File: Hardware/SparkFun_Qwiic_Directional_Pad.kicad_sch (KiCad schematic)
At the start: 36 parts, among them J1 Qwiic_RA, J2 Conn_01x04, J3 Qwiic_RA, J5 I2C, SW2 Nav Switch, U4 PCA9557PW

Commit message: Add ignore
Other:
- note added: "Default I²C Address: 0x18"
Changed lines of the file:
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@@
+		)
+	)
+	(text "Default I²C Address: 0x18"
+		(exclude_from_sim no)
+		(at 190.5 86.36 0)
+		(effects
+			(font
+				(size 1.27 1.27)
+			)
 		)
 	)

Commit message: Fix page names.
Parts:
- added JP6: I²C, SparkFun-Jumper:Jumper_3_NC-2_Trace, symbol SparkFun-Jumper:SolderJumper_3_Bridged123
- added R13, R7: 2.2k, SparkFun-Resistor:R_0603_1608Metric, symbol SparkFun-Resistor:2.2k_0603
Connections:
- net 3.3V: now also JP6.2 (C)
- net SCL: now also R7.2
- net SDA: now also R13.2
- new net: JP6.1 (A), R13.1
- new net: JP6.3 (B), R7.1
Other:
- title: RTK Postcard Portable Shield -> SparkFun Qwiic Directional Pad
- moved on the sheet: C1, D1, D4, J1, J2, J3, J5, JP1, JP2, JP3, R1, R10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

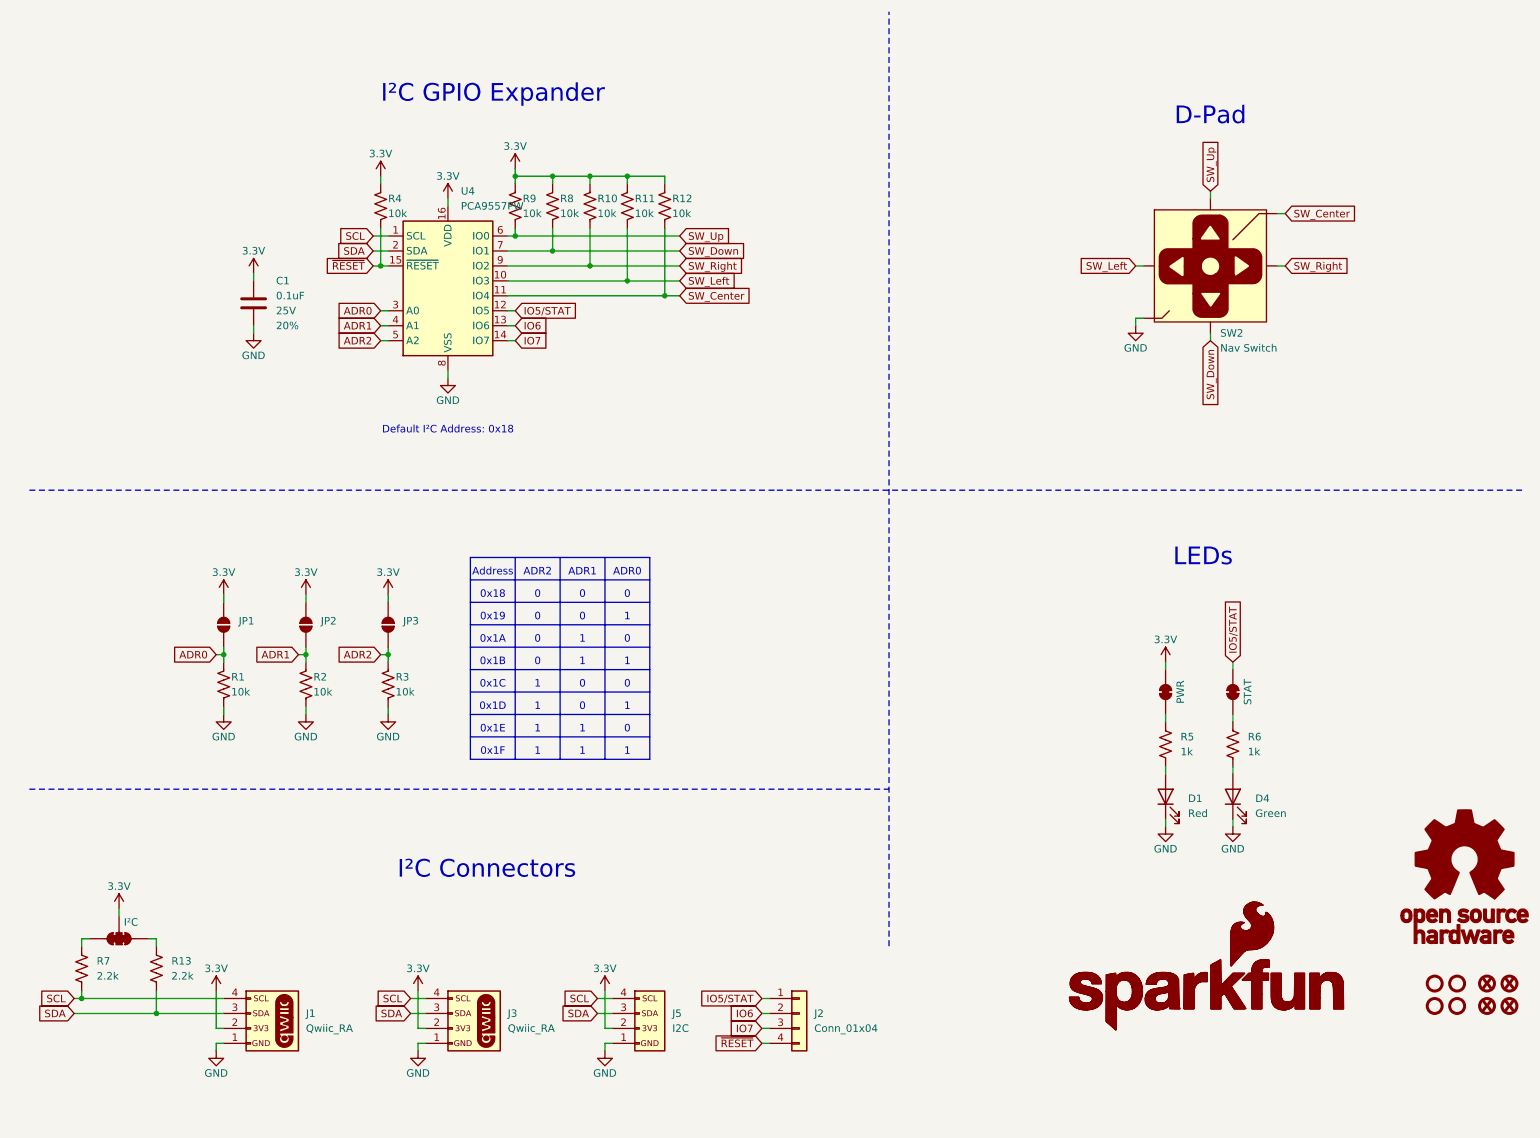
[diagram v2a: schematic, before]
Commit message: Switch to RGB 1205 rear mount LED
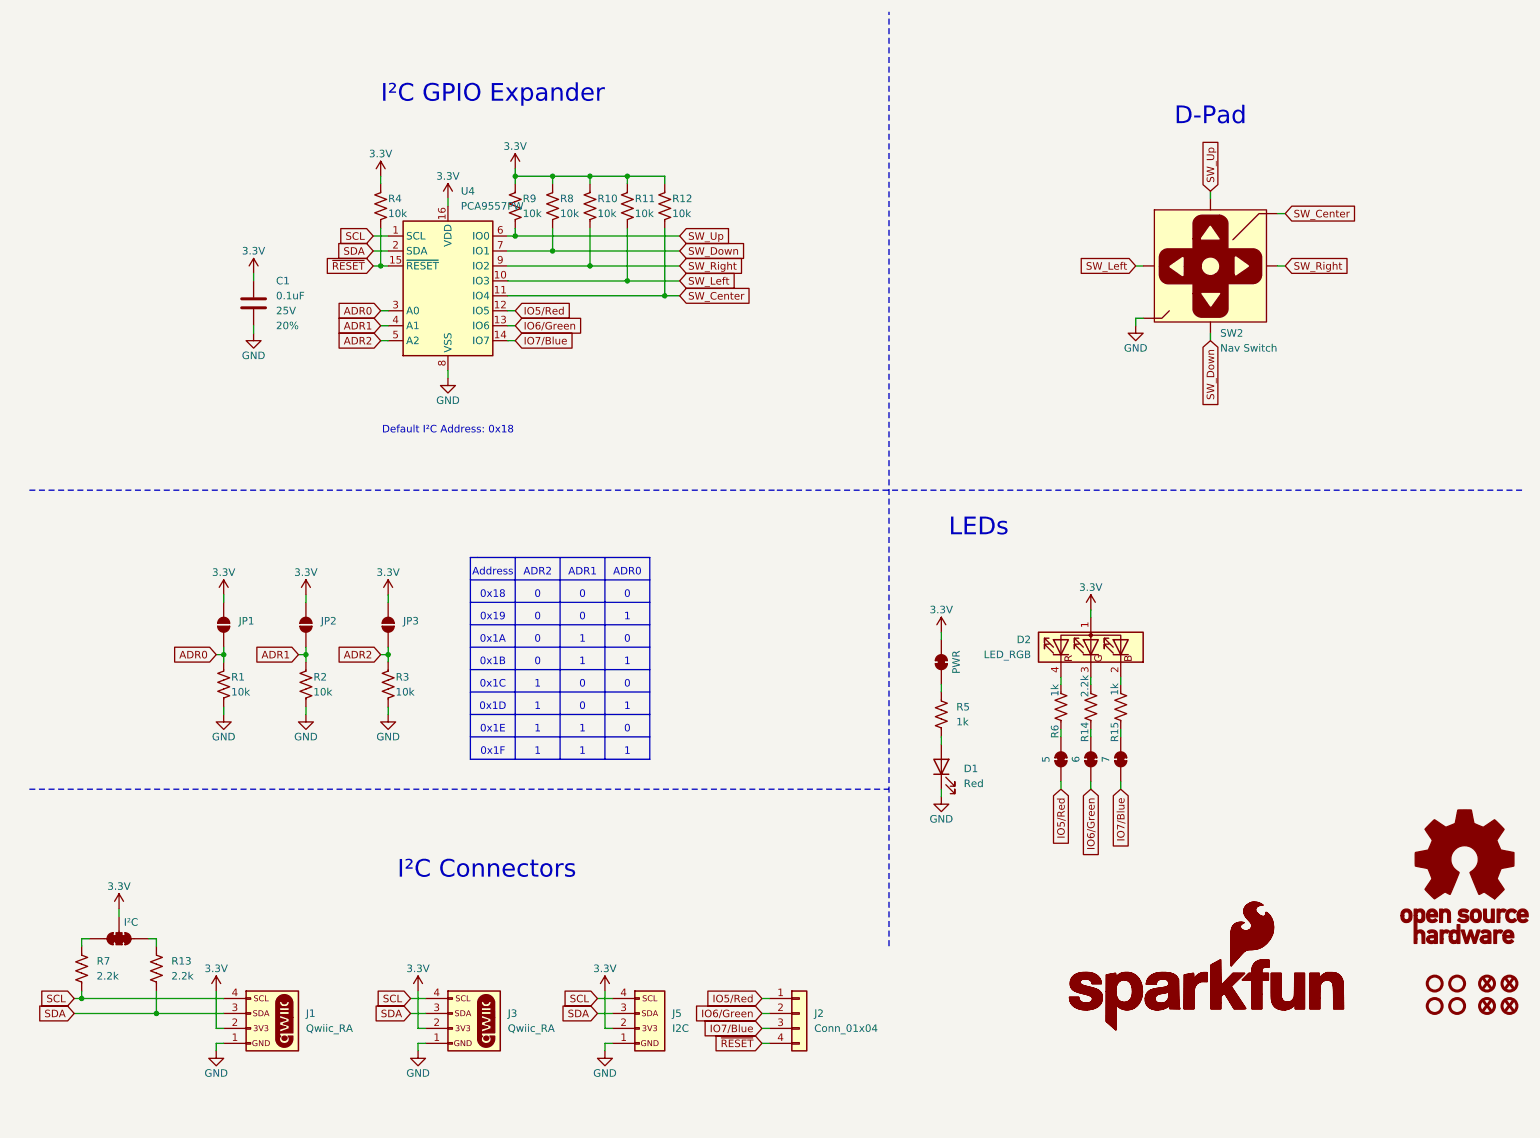
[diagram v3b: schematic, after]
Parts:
- removed D4: Green, SparkFun-LED:LED_1206_Bottom_Green, symbol SparkFun-LED:LED_Green_1206-Bottom
- added D2: LED_RGB, SparkFun-LED:LED_1205_RGB_Bottom, symbol SparkFun-LED:LED_RGB_1205_Bottom
- added JP7: 6, SparkFun-Jumper:Jumper_2_NC_Trace, symbol SparkFun-Jumper:SolderJumper_2_Bridged
- added JP8: 7, SparkFun-Jumper:Jumper_2_NC_Trace, symbol SparkFun-Jumper:SolderJumper_2_Bridged
- added R14: 2.2k, SparkFun-Resistor:R_0603_1608Metric, symbol SparkFun-Resistor:2.2k_0603
- added R15: 1k, SparkFun-Resistor:R_0603_1608Metric, symbol SparkFun-Resistor:1k_0603
- JP5: value STAT -> 5
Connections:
- net 3.3V: now also D2.1 (A)
- net at R6.2: now also D2.4 (RK)
- net IO5/STAT renamed IO5/Red
- net IO6 renamed IO6/Green
- net IO6/Green: now also JP7.2 (B)
- net IO7 renamed IO7/Blue
- net IO7/Blue: now also JP8.2 (B)
- new net: JP7.1 (A), R14.1
- new net: D2.3 (GK), R14.2
- new net: D2.2 (BK), R15.2
- new net: JP8.1 (A), R15.1
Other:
- moved on the sheet: D1, R5

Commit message: Switch to PCA9554
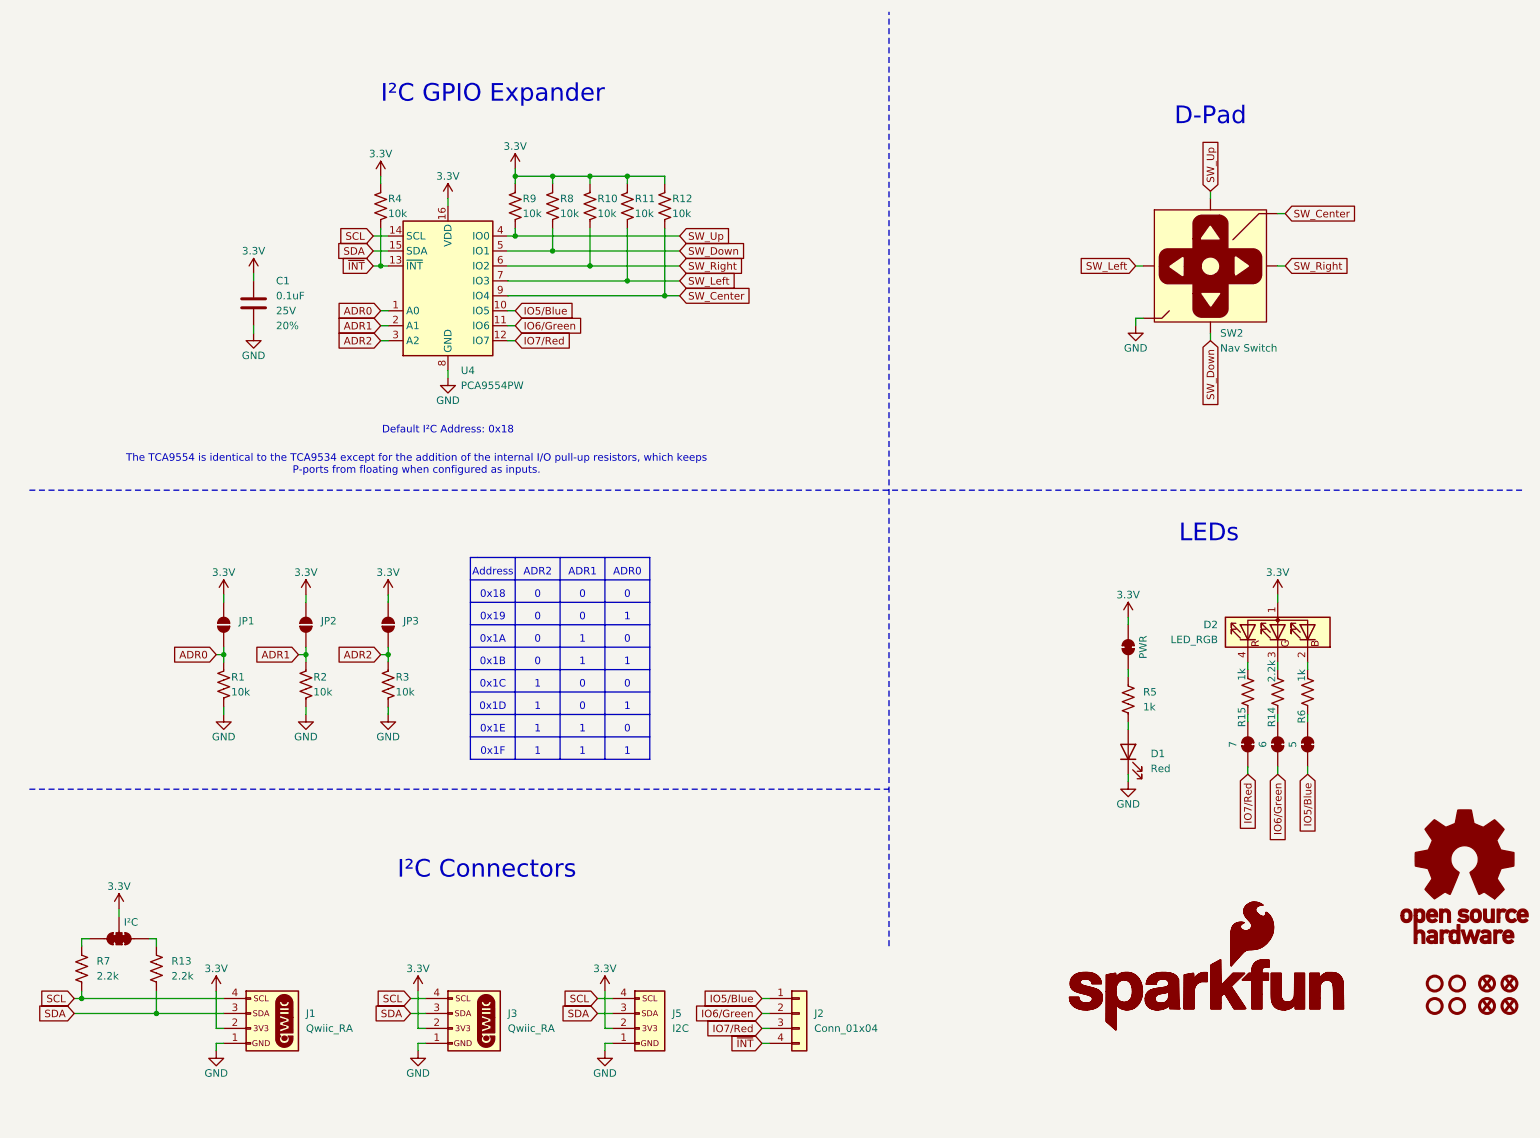
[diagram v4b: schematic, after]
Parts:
- SW2: PROD_ID SWCH-12265 -> SWCH-23356
- U4: value PCA9557PW -> PCA9554PW; symbol SparkFun-IC-Special-Function:PCA9557PW -> SparkFun-IC-Special-Function:PCA9554PW; PROD_ID IC-23355 -> IC-23589
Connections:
- net ADR0: now also U4.1 (A0); no longer U4.3 (A0)
- net ADR1: now also U4.2 (A1); no longer U4.4 (A1)
- net ADR2: now also U4.3 (A2); no longer U4.5 (A2)
- net IO6/Green: now also U4.11 (IO6); no longer U4.13 (IO6)
- net SCL: now also U4.14 (SCL); no longer U4.1 (SCL)
- net SDA: now also U4.15 (SDA); no longer U4.2 (SDA)
- net SW_Center: now also U4.9 (IO4); no longer U4.11 (IO4)
- net SW_Down: now also U4.5 (IO1); no longer U4.7 (IO1)
- net SW_Left: now also U4.7 (IO3); no longer U4.10 (IO3)
- net SW_Right: now also U4.6 (IO2); no longer U4.9 (IO2)
- net SW_Up: now also U4.4 (IO0); no longer U4.6 (IO0)
- net at D2.2 (BK): now also R6.2; no longer R15.2
- net at D2.4 (RK): now also R15.2; no longer R6.2
- net IO5/Red renamed IO5/Blue
- net IO5/Blue: now also U4.10 (IO5); no longer U4.12 (IO5)
- net IO7/Blue renamed IO7/Red
- net IO7/Red: now also U4.12 (IO7); no longer U4.14 (IO7)
- net ~{RESET} renamed ~{INT}
- net ~{INT}: now also U4.13 (~{INT}); no longer U4.15 (~{RESET})
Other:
- note added: "The TCA9554 is identical to the TCA9534 except for the addition of the internal I/O pull-up resistors, which keeps P-ports from floating when configured as inputs."
- moved on the sheet: D1, D2, R14, R15, R5, R6

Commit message: Switch to PCA9554 with INT pin
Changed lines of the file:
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@@
 	(title_block
 		(title "SparkFun Qwiic Directional Pad")
-		(date "2024-09-23")
-		(rev "v10")
+		(date "2024-10-17")
+		(rev "v11")
 		(comment 1 "Designed by: N. Seidle")
 	)

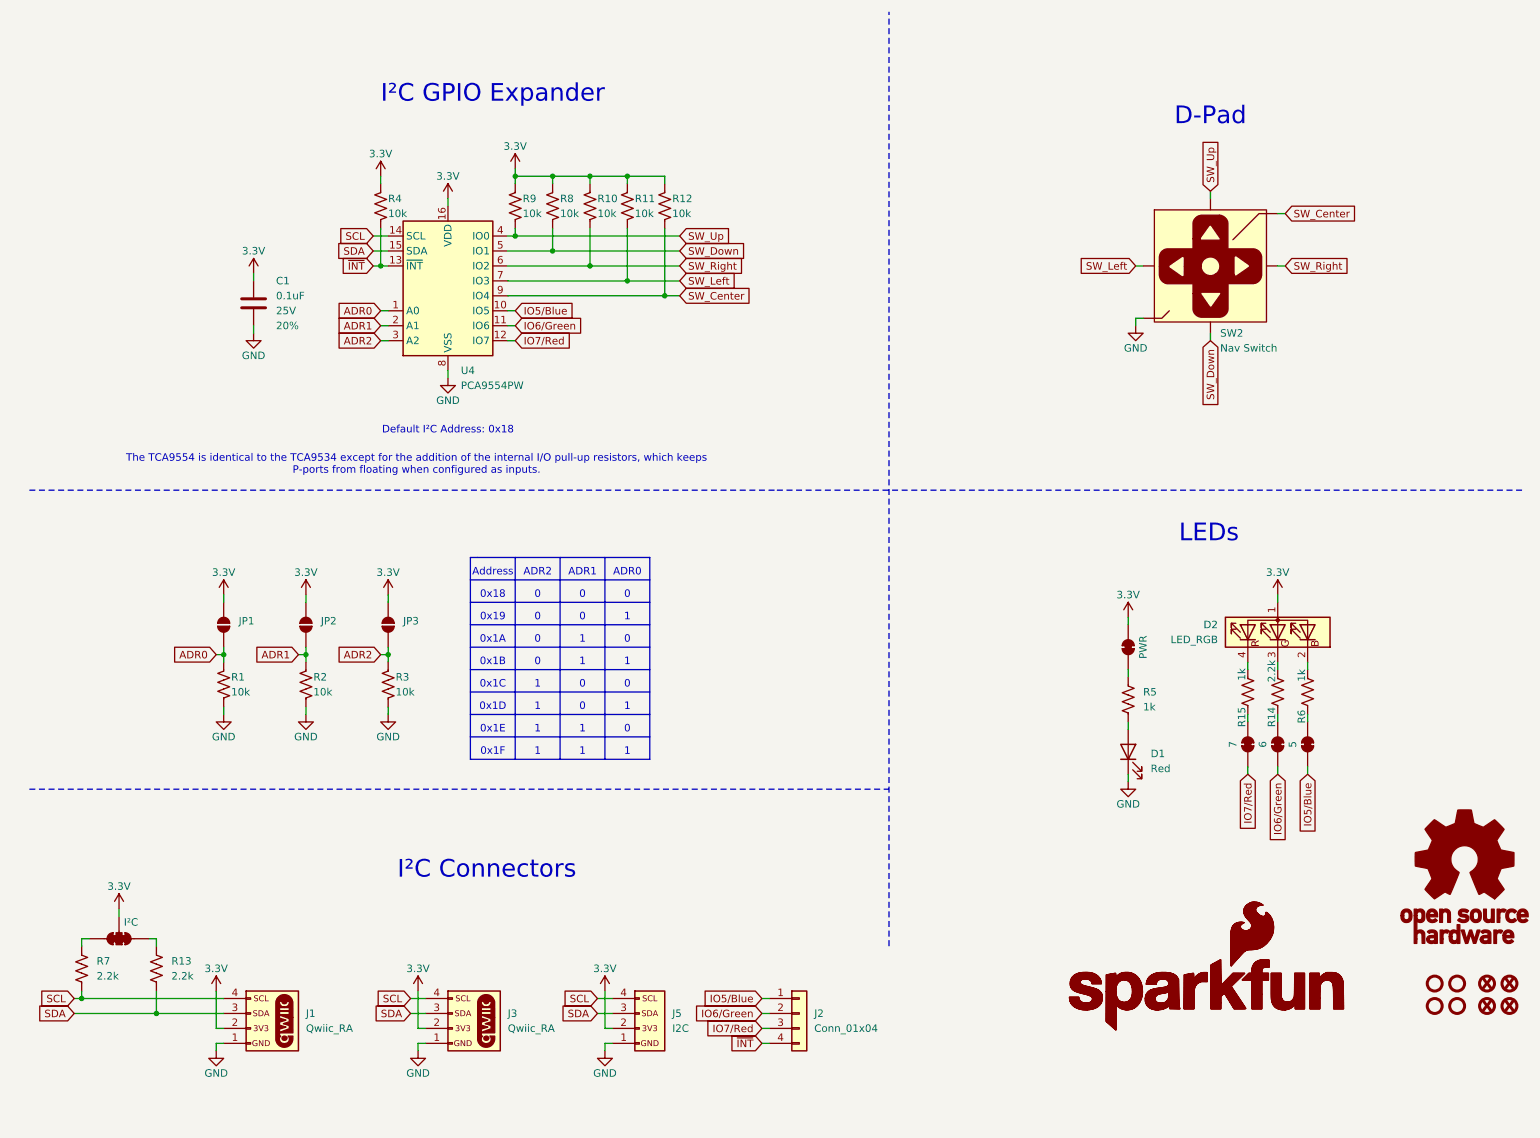
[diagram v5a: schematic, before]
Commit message: Update jumper names, I2C address table.
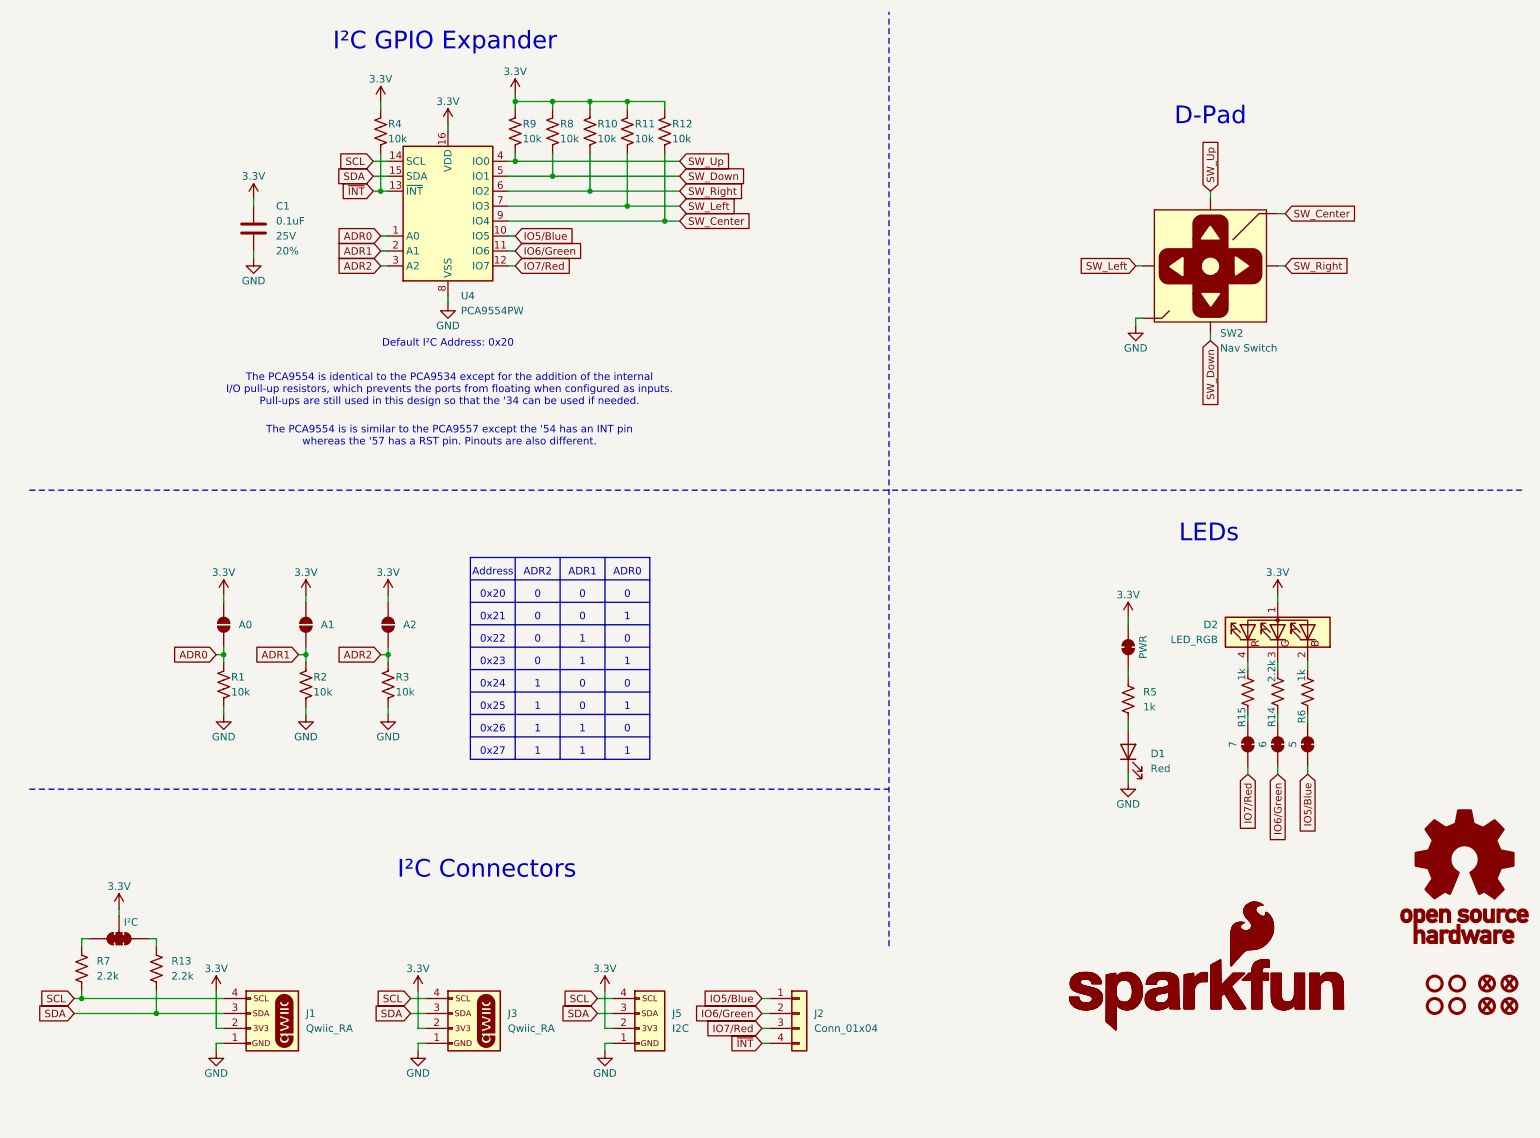
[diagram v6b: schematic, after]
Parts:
- JP1: value ~ -> A0
- JP2: value ~ -> A1
- JP3: value ~ -> A2
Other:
- note added: "0x20"
- note added: "0x21"
- note added: "0x22"
- note added: "0x23"
- note added: "0x24"
- note added: "0x25"
- note added: "0x26"
- note added: "0x27"
- note added: "Default I²C Address: 0x20"
- note added: "The PCA9554 is identical to the PCA9534 except for the addition of the internal I/O pull-up resistors, which prevents the ports from floating when configured as inputs. Pull-ups are still used in this design so that the '34 can be used if needed."
- note added: "The PCA9554 is is similar to the PCA9557 except the '54 has an INT pin whereas the '57 has a RST pin. Pinouts are also different."
- note removed: "0x18"
- note removed: "0x19"
- note removed: "0x1A"
- note removed: "0x1B"
- note removed: "0x1C"
- note removed: "0x1D"
- note removed: "0x1E"
- note removed: "0x1F"
- note removed: "Default I²C Address: 0x18"
- note removed: "The TCA9554 is identical to the TCA9534 except for the addition of the internal I/O pull-up resistors, which keeps P-ports from floating when configured as inputs."
- moved on the sheet: C1, R10, R11, R12, R4, R8, R9, U4
